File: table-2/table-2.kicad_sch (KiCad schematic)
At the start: 34 parts, among them J1 1.8" OLED DISPLAY, J10 LED Strip Connector, J2 Barrel_Jack, J3 MPU6050, J4 Ultrasonic Sensor, J5 USB_A, J6 USB_A, J7 Dual H-Bridge Control, J8 USB_C_Receptacle_PowerOnly_6P, J9 Dual H-Brdige Power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

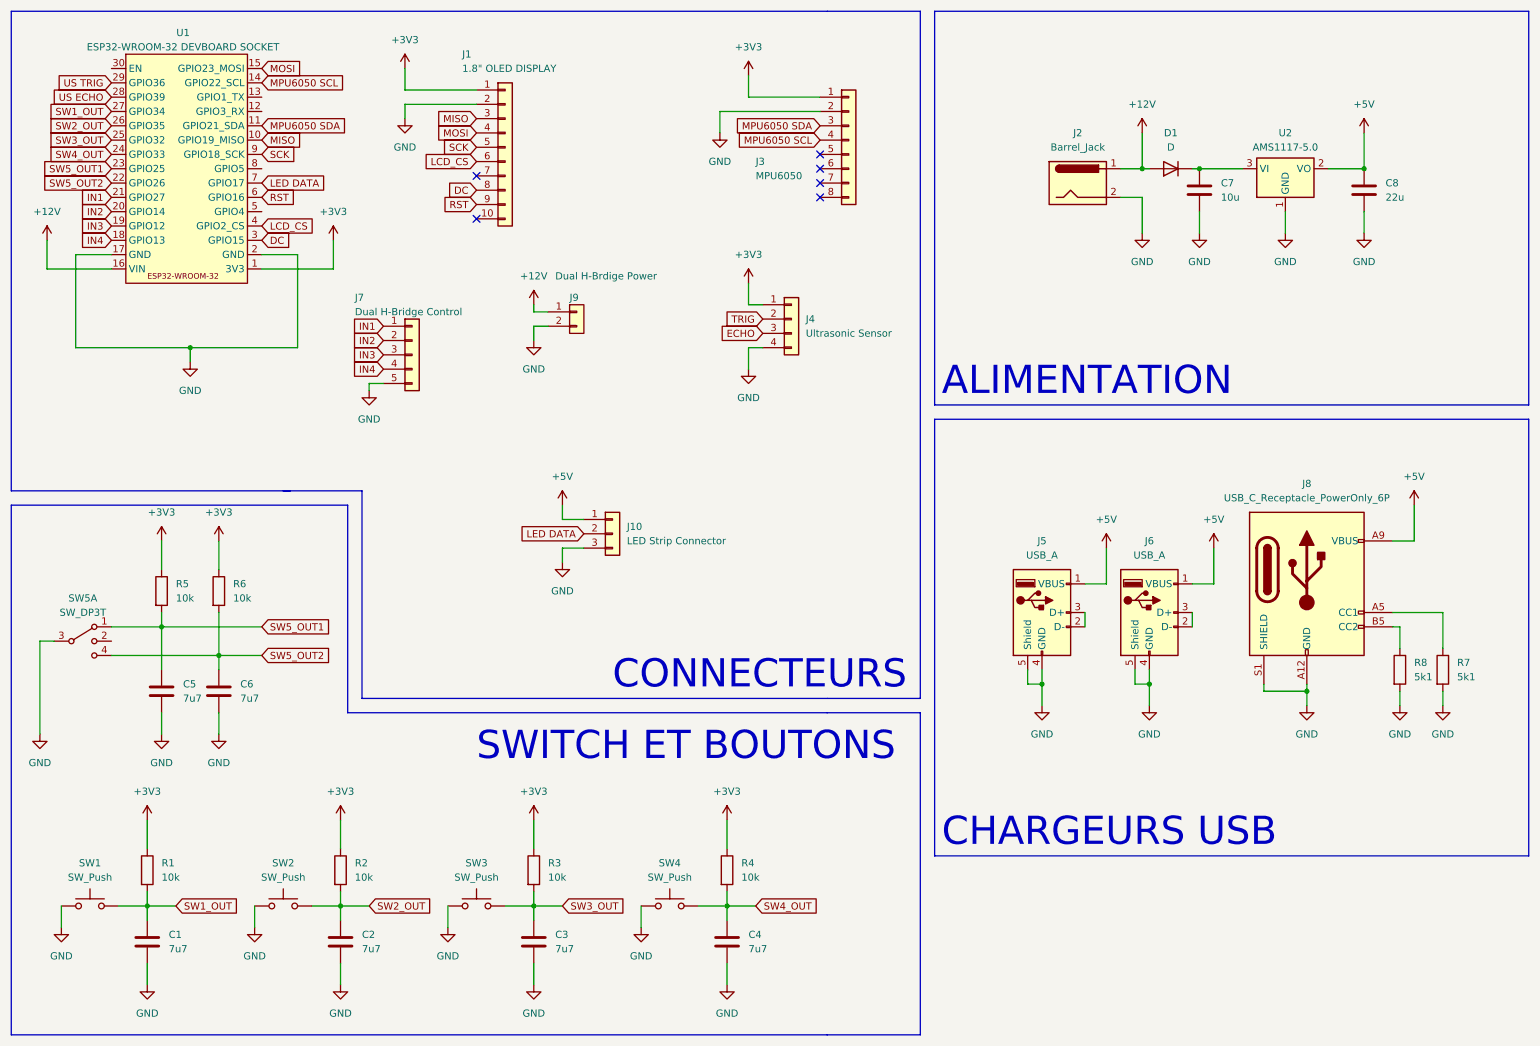
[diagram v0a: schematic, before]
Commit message: added footprints, changed volt reg, changed toggle switch, and more
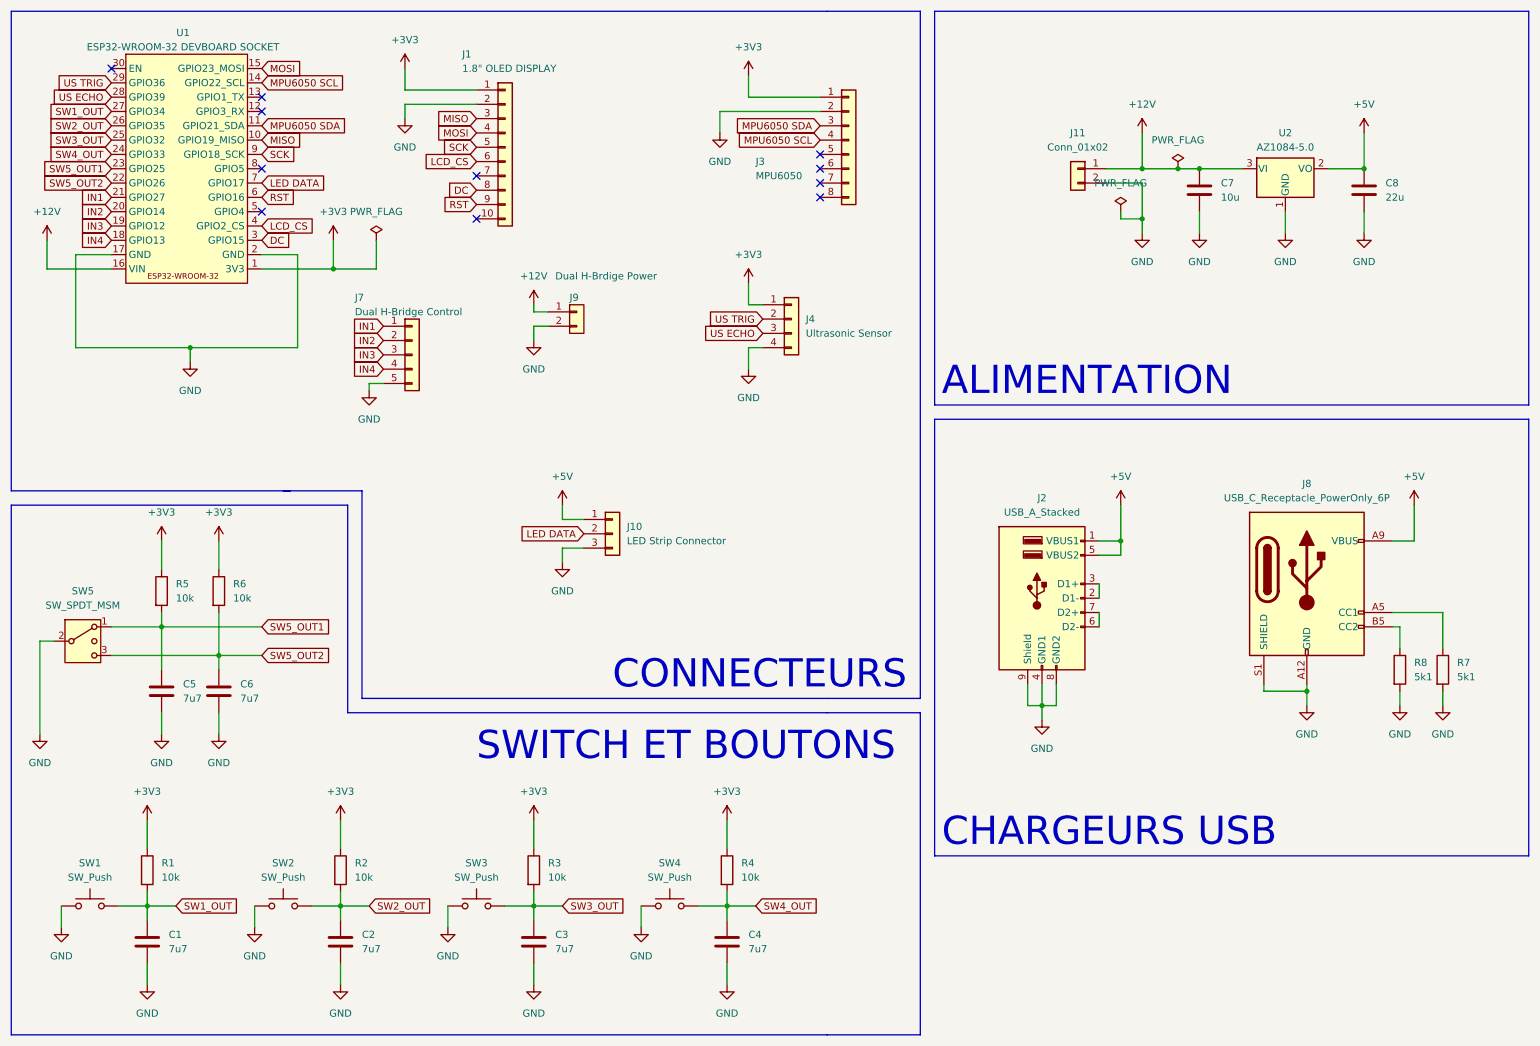
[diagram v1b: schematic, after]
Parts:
- removed D1: D, symbol Device:D
- removed J2: Barrel_Jack, symbol Connector:Barrel_Jack
- removed J5, J6: USB_A, symbol Connector:USB_A
- removed SW5: SW_DP3T, symbol Switch:SW_DP3T
- removed U2: AMS1117-5.0, Package_TO_SOT_SMD:SOT-223-3_TabPin2, symbol Regulator_Linear:AMS1117-5.0
- added J11: Conn_01x02, TerminalBlock:TerminalBlock_Wuerth_691311400102_P7.62mm, symbol Connector_Generic:Conn_01x02
- added J2: USB_A_Stacked, Connector_USB:USB_A_CUI_UJ2-ADH-TH_Horizontal_Stacked, symbol Connector:USB_A_Stacked
- added SW5: SW_SPDT_MSM, JiaLib:BST13T1AVR, symbol Switch:SW_SPDT_MSM
- added U2: AZ1084-5.0, JiaLib:AZ1084CD-5.0TRG1, symbol Regulator_Linear:AZ1084-5.0
- C7, C8: footprint (none) -> Capacitor_SMD:C_0805_2012Metric_Pad1.18x1.45mm_HandSolder
- J1: footprint (none) -> Connector_PinHeader_2.54mm:PinHeader_1x10_P2.54mm_Vertical
- J10: footprint (none) -> Connector_PinHeader_2.54mm:PinHeader_1x03_P2.54mm_Vertical
- J3: footprint (none) -> Connector_PinHeader_2.54mm:PinHeader_1x08_P2.54mm_Vertical
- J4: footprint (none) -> Connector_PinHeader_2.54mm:PinHeader_1x04_P2.54mm_Vertical
- J7: footprint (none) -> Connector_PinHeader_2.54mm:PinHeader_1x05_P2.54mm_Vertical
- J8: footprint (none) -> Connector_USB:USB_C_Receptacle_GCT_USB4125-xx-x-0190_6P_TopMnt_Horizontal
- J9: footprint 0CSL_D1_V1:Molex_PicoBlade_P1.25mm_HorAG -> TerminalBlock:TerminalBlock_Wuerth_691311400102_P7.62mm
- R7, R8: footprint (none) -> Resistor_SMD:R_0805_2012Metric_Pad1.20x1.40mm_HandSolder
- SW1, SW2, SW3, SW4: footprint (none) -> 0CSL_D1_V1:Tactile_90_TE
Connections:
- net ECHO is gone; now on net US ECHO: J4.3 (Pin_3)
- net TRIG is gone; now on net US TRIG: J4.2 (Pin_2)
- net +12V: now also C7.1, J11.1 (Pin_1), U2.3 (VI)
- net +5V: now also J2.1 (VBUS1), J2.5 (VBUS2), U2.2 (VO)
- net GND: now also J11.2 (Pin_2), J2.4 (GND1), J2.8 (GND2), J2.9 (Shield), SW5.2 (3), U2.1 (GND)
- net SW5_OUT1: now also SW5.1
- net SW5_OUT2: now also SW5.3 (4)
- new net: J2.2 (D1-), J2.3 (D1+)
- new net: J2.6 (D2-), J2.7 (D2+)
- no-connect marks 6 -> 11
